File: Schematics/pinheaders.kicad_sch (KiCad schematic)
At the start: 20 parts, among them J1001 Conn_01x08_Pin, J1002 Conn_01x08_Pin, J1003 Conn_01x08_Pin, J1004 Conn_01x08_Pin, J1005 Conn_01x08_Pin, J1006 Conn_01x16_Pin, J1007 Conn_01x16_Pin, J1008 Conn_01x08_Pin, J1009 Conn_01x08_Pin, J1010 Conn_01x08_Pin, J1011 Conn_01x08_Pin, J1012 Conn_01x08_Pin, J1013 Conn_01x08_Pin, J1014 Conn_01x08_Pin, J1015 Conn_01x08_Pin, J1016 Conn_01x08_Pin, J1017 Conn_01x08_Pin, J1018 Conn_01x08_Pin, J1019 Conn_01x08_Pin, J1020 Conn_01x08_Pin

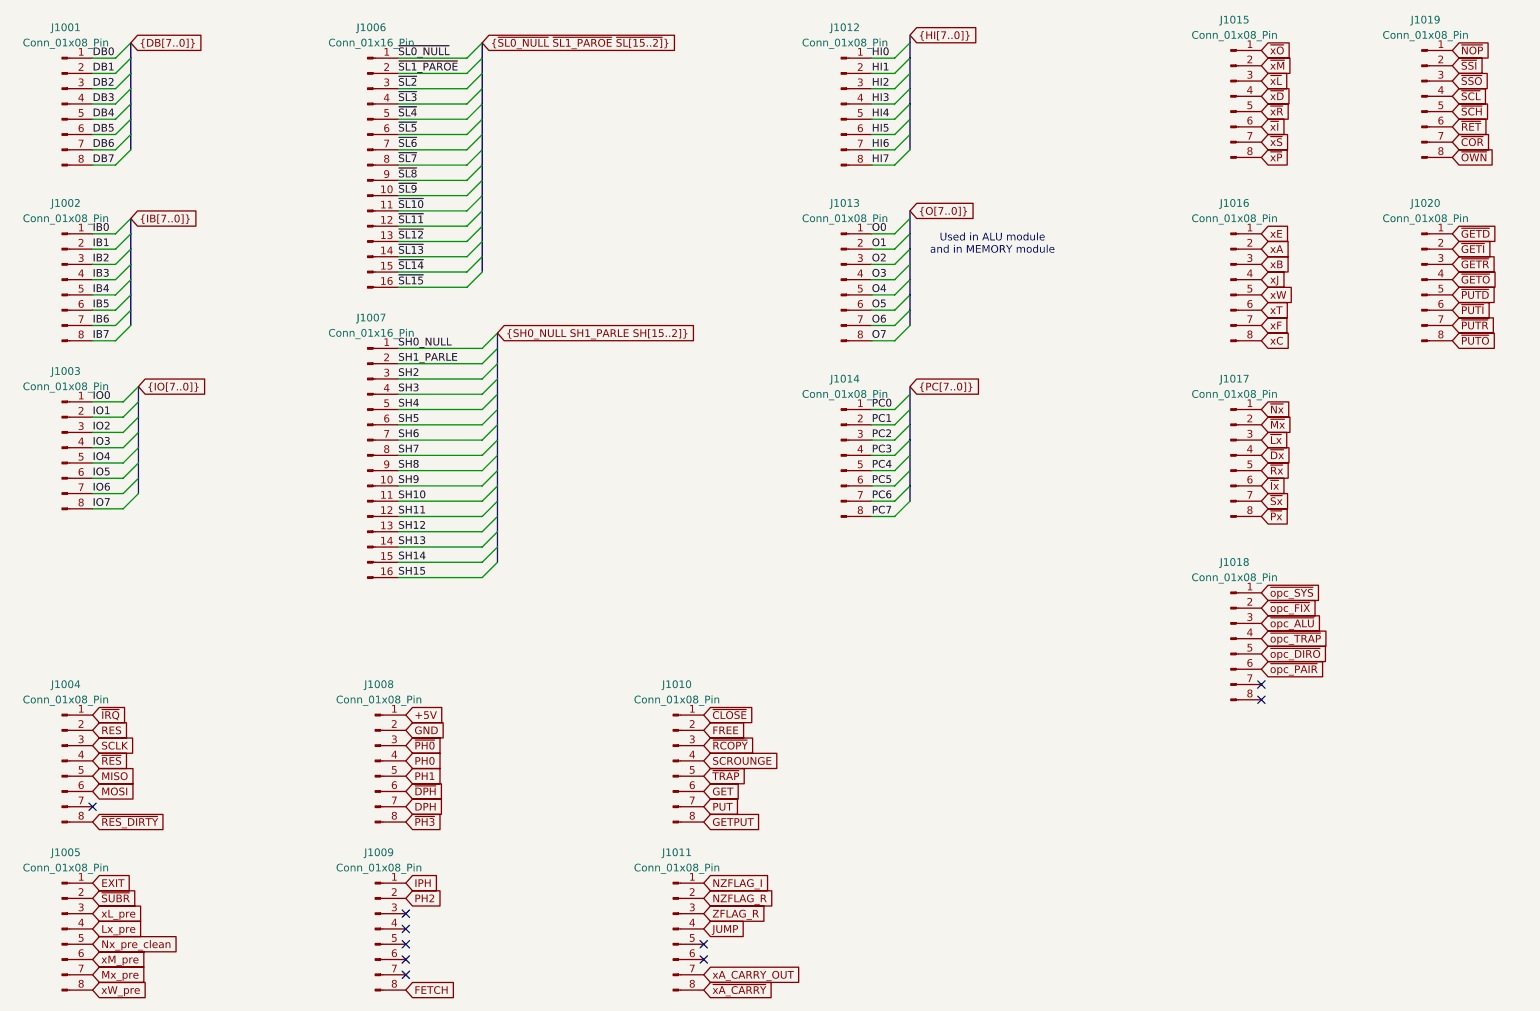
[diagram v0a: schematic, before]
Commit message: Reduce number of shared headers
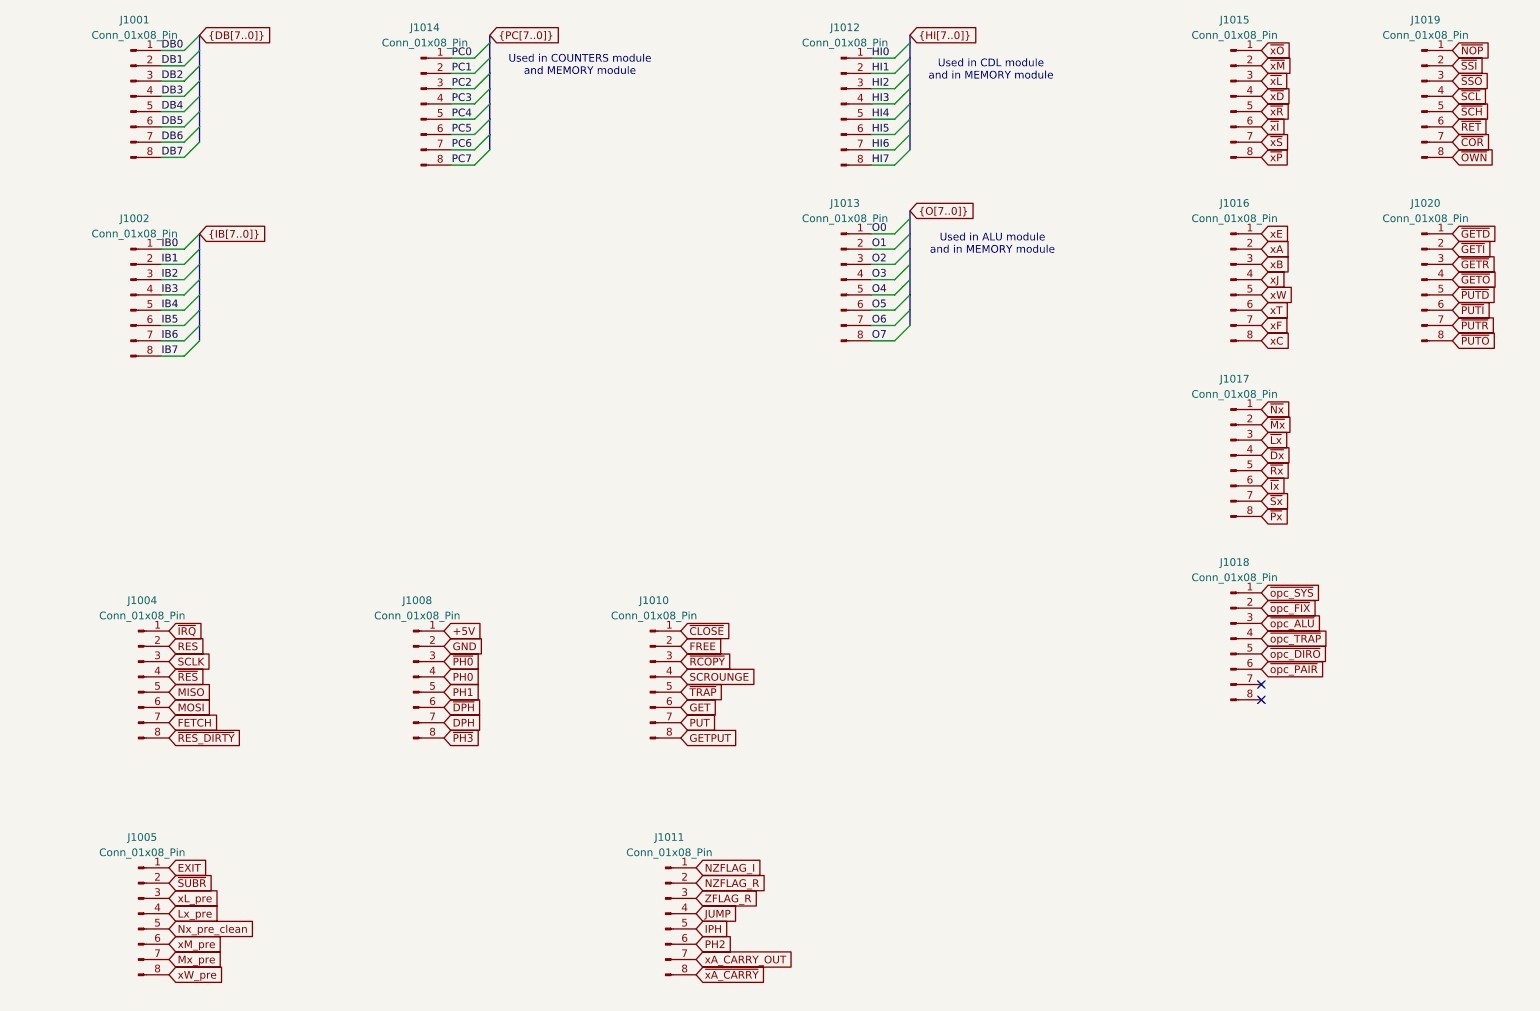
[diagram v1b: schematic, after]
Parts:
- removed J1003: Conn_01x08_Pin, symbol Connector:Conn_01x08_Pin
- removed J1006, J1007: Conn_01x16_Pin, Connector_PinHeader_2.54mm:PinHeader_1x16_P2.54mm_Vertical, symbol Connector:Conn_01x16_Pin
- removed J1009: Conn_01x08_Pin, Connector_PinHeader_2.54mm:PinHeader_1x08_P2.54mm_Vertical, symbol Connector:Conn_01x08_Pin
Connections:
- net FETCH: now also J1004.7 (Pin_7)
- net IPH: now also J1011.5 (Pin_5)
- net PH2: now also J1011.6 (Pin_6)
- no-connect marks 10 -> 2
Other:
- note added: "Used in CDL module and in MEMORY module"
- note added: "Used in COUNTERS module and MEMORY module"
- moved on the sheet: J1001, J1002, J1004, J1005, J1008, J1010, J1011, J1014

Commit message: Change d to g
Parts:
- J1001, J1002, J1004, J1008, J1010, J1011, J1012, J1014, J1015, J1016, J1017, J1018, J1019, J1020: footprint (none) -> Connector_PinHeader_2.54mm:PinHeader_1x08_P2.54mm_Vertical
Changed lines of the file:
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@@
 			)
 		)
-		(property "Footprint" ""
+		(property "Footprint" "Connector_PinHeader_2.54mm:PinHeader_1x08_P2.54mm_Vertical"
 			(at 220.98 31.75 0)
 			(effects
@@
 			(project "myth_decoder"
 				(path "/cc431572-b987-4113-b719-2952a6ee3168/4a47d886-11a5-4437-bd08-9d99b37632a9"
-					(reference "J1015")
+					(reference "J1011")
 					(unit 1)
 				)
@@
 			)
 		)
-		(property "Footprint" ""
+		(property "Footprint" "Connector_PinHeader_2.54mm:PinHeader_1x08_P2.54mm_Vertical"
 			(at 127 167.64 0)
 			(effects
@@
 			(project "myth_decoder"
 				(path "/cc431572-b987-4113-b719-2952a6ee3168/4a47d886-11a5-4437-bd08-9d99b37632a9"
-					(reference "J1011")
+					(reference "J1008")
 					(unit 1)
 				)
@@
 			)
 		)
-		(property "Footprint" ""
+		(property "Footprint" "Connector_PinHeader_2.54mm:PinHeader_1x08_P2.54mm_Vertical"
 			(at 220.98 62.23 0)
 			(effects
@@
 			(project "myth_decoder"
 				(path "/cc431572-b987-4113-b719-2952a6ee3168/4a47d886-11a5-4437-bd08-9d99b37632a9"
-					(reference "J1016")
+					(reference "J1012")
 					(unit 1)
 				)
@@
 			)
 		)
-		(property "Footprint" ""
+		(property "Footprint" "Connector_PinHeader_2.54mm:PinHeader_1x08_P2.54mm_Vertical"
 			(at 85.09 128.27 0)
 			(effects
@@
 			(project "myth_decoder"
 				(path "/cc431572-b987-4113-b719-2952a6ee3168/4a47d886-11a5-4437-bd08-9d99b37632a9"
-					(reference "J1008")
+					(reference "J1005")
 					(unit 1)
 				)
@@
 			)
 		)
-		(property "Footprint" ""
+		(property "Footprint" "Connector_PinHeader_2.54mm:PinHeader_1x08_P2.54mm_Vertical"
 			(at 38.1 31.75 0)
 			(effects
@@
 			)
 		)
-		(property "Footprint" ""
+		(property "Footprint" "Connector_PinHeader_2.54mm:PinHeader_1x08_P2.54mm_Vertical"
 			(at 38.1 64.77 0)
 			(effects
@@
 			)
 		)
-		(property "Footprint" ""
+		(property "Footprint" "Connector_PinHeader_2.54mm:PinHeader_1x08_P2.54mm_Vertical"
 			(at 252.73 31.75 0)
 			(effects
@@
 			(project "myth_decoder"
 				(path "/cc431572-b987-4113-b719-2952a6ee3168/4a47d886-11a5-4437-bd08-9d99b37632a9"
-					(reference "J1019")
+					(reference "J1015")
 					(unit 1)
 				)
@@
 			)
 		)
-		(property "Footprint" ""
+		(property "Footprint" "Connector_PinHeader_2.54mm:PinHeader_1x08_P2.54mm_Vertical"
 			(at 124.46 128.27 0)
 			(effects
@@
 			(project "myth_decoder"
 				(path "/cc431572-b987-4113-b719-2952a6ee3168/4a47d886-11a5-4437-bd08-9d99b37632a9"
-					(reference "J1010")
+					(reference "J1007")
 					(unit 1)
 				)
@@
 			)
 		)
-		(property "Footprint" ""
+		(property "Footprint" "Connector_PinHeader_2.54mm:PinHeader_1x08_P2.54mm_Vertical"
 			(at 220.98 91.44 0)
 			(effects
@@
 			(project "myth_decoder"
 				(path "/cc431572-b987-4113-b719-2952a6ee3168/4a47d886-11a5-4437-bd08-9d99b37632a9"
-					(reference "J1017")
+					(reference "J1013")
 					(unit 1)
 				)
@@
 			)
 		)
-		(property "Footprint" ""
+		(property "Footprint" "Connector_PinHeader_2.54mm:PinHeader_1x08_P2.54mm_Vertical"
 			(at 156.21 33.02 0)
 			(effects
@@
 			(project "myth_decoder"
 				(path "/cc431572-b987-4113-b719-2952a6ee3168/4a47d886-11a5-4437-bd08-9d99b37632a9"
-					(reference "J1012")
+					(reference "J1009")
 					(unit 1)
 				)
@@
 			)
 		)
-		(property "Footprint" ""
+		(property "Footprint" "Connector_PinHeader_2.54mm:PinHeader_1x08_P2.54mm_Vertical"
 			(at 39.37 128.27 0)
 			(effects
@@
 			(project "myth_decoder"
 				(path "/cc431572-b987-4113-b719-2952a6ee3168/4a47d886-11a5-4437-bd08-9d99b37632a9"
-					(reference "J1004")
+					(reference "J1003")
 					(unit 1)
 				)
@@
 			(project "myth_decoder"
 				(path "/cc431572-b987-4113-b719-2952a6ee3168/4a47d886-11a5-4437-bd08-9d99b37632a9"
-					(reference "J1005")
+					(reference "J1004")
 					(unit 1)
 				)
@@
 			)
 		)
-		(property "Footprint" ""
+		(property "Footprint" "Connector_PinHeader_2.54mm:PinHeader_1x08_P2.54mm_Vertical"
 			(at 220.98 121.92 0)
 			(effects
@@
 			(project "myth_decoder"
 				(path "/cc431572-b987-4113-b719-2952a6ee3168/4a47d886-11a5-4437-bd08-9d99b37632a9"
-					(reference "J1018")
+					(reference "J1014")
 					(unit 1)
 				)
@@
 			(project "myth_decoder"
 				(path "/cc431572-b987-4113-b719-2952a6ee3168/4a47d886-11a5-4437-bd08-9d99b37632a9"
-					(reference "J1013")
+					(reference "J1010")
 					(unit 1)
 				)
@@
 			)
 		)
-		(property "Footprint" ""
+		(property "Footprint" "Connector_PinHeader_2.54mm:PinHeader_1x08_P2.54mm_Vertical"
 			(at 252.73 62.23 0)
 			(effects
@@
 			(project "myth_decoder"
 				(path "/cc431572-b987-4113-b719-2952a6ee3168/4a47d886-11a5-4437-bd08-9d99b37632a9"
-					(reference "J1020")
+					(reference "J1016")
 					(unit 1)
 				)
@@
 			)
 		)
-		(property "Footprint" ""
+		(property "Footprint" "Connector_PinHeader_2.54mm:PinHeader_1x08_P2.54mm_Vertical"
 			(at 86.36 33.02 0)
 			(effects
@@
 			(project "myth_decoder"
 				(path "/cc431572-b987-4113-b719-2952a6ee3168/4a47d886-11a5-4437-bd08-9d99b37632a9"
-					(reference "J1014")
-					(unit 1)
-				)
+					(reference "J1006")
+					(unit 1)
+				)

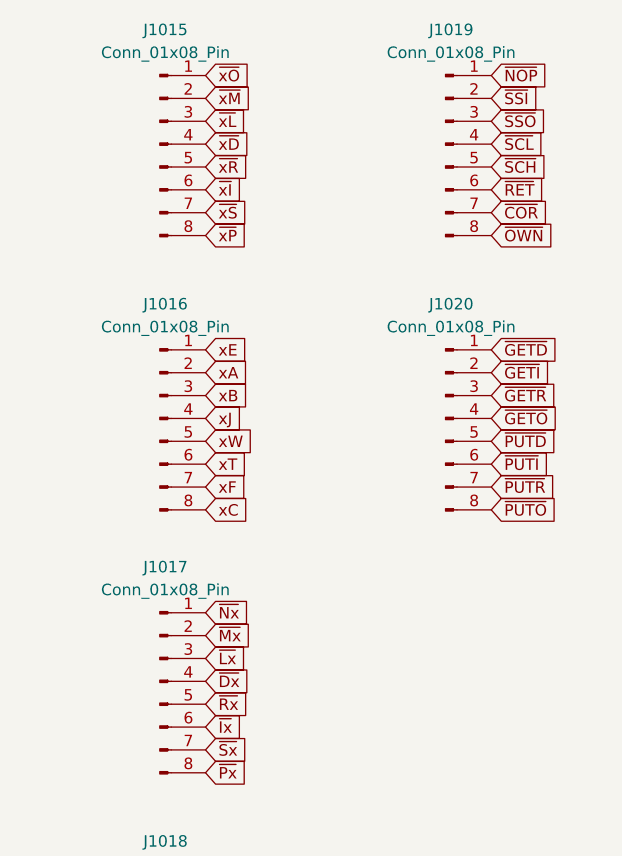
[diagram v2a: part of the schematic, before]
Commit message: Change CO do D
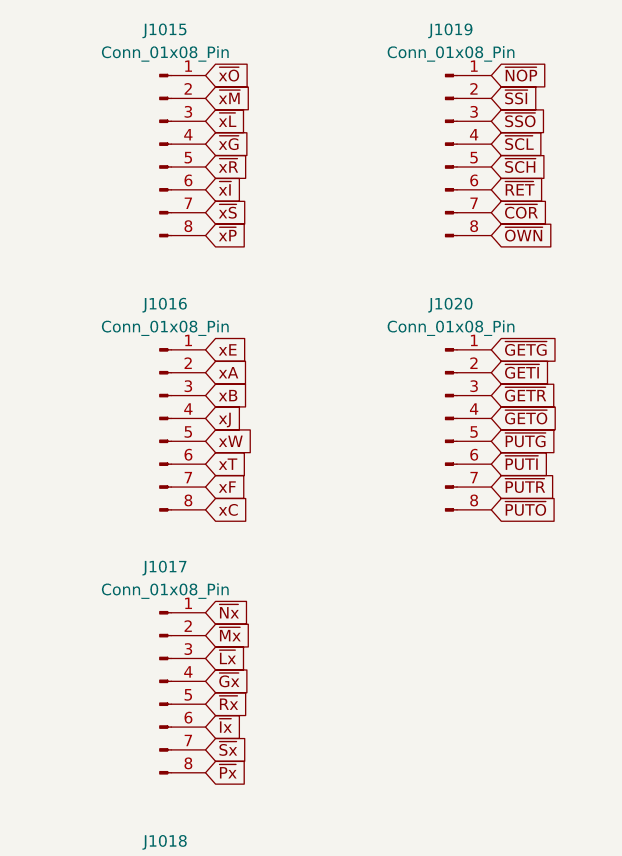
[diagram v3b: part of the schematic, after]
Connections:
- net ~{Dx} renamed ~{Gx}
- net ~{GETD} renamed ~{GETG}
- net ~{PUTD} renamed ~{PUTG}
- net ~{xD} renamed ~{xG}
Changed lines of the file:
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@@
 		)
 	)
-	(global_label "~{Dx}"
+	(global_label "~{Gx}"
 		(shape input)
 		(at 226.06 91.44 0)
@@
 		)
 	)
-	(global_label "~{PUTD}"
+	(global_label "~{PUTG}"
 		(shape input)
 		(at 257.81 64.77 0)
@@
 		)
 	)
-	(global_label "~{GETD}"
+	(global_label "~{GETG}"
 		(shape input)
 		(at 257.81 54.61 0)
@@
 		)
 	)
-	(global_label "~{xD}"
+	(global_label "~{xG}"
 		(shape input)
 		(at 226.06 31.75 0)
@@
 			(project "myth_io"
 				(path "/a907dd88-e0e4-4e6e-a291-053f6213a316/95b8575f-ea13-4da8-aaa7-78fdcde116f0"
-					(reference "J1011")
+					(reference "J1012")
 					(unit 1)
 				)
@@
 			(project "myth_io"
 				(path "/a907dd88-e0e4-4e6e-a291-053f6213a316/95b8575f-ea13-4da8-aaa7-78fdcde116f0"
-					(reference "J1008")
+					(reference "J1009")
 					(unit 1)
 				)
@@
 			(project "myth_io"
 				(path "/a907dd88-e0e4-4e6e-a291-053f6213a316/95b8575f-ea13-4da8-aaa7-78fdcde116f0"
-					(reference "J1001")
+					(reference "J1005")
 					(unit 1)
 				)
@@
 			(project "myth_io"
 				(path "/a907dd88-e0e4-4e6e-a291-053f6213a316/95b8575f-ea13-4da8-aaa7-78fdcde116f0"
-					(reference "J1002")
+					(reference "J1006")
 					(unit 1)
 				)
@@
 			(project "myth_io"
 				(path "/a907dd88-e0e4-4e6e-a291-053f6213a316/95b8575f-ea13-4da8-aaa7-78fdcde116f0"
-					(reference "J1010")
+					(reference "J1011")
 					(unit 1)
 				)
@@
 			(project "myth_io"
 				(path "/a907dd88-e0e4-4e6e-a291-053f6213a316/95b8575f-ea13-4da8-aaa7-78fdcde116f0"
-					(reference "J1012")
+					(reference "J1013")
 					(unit 1)
 				)
@@
 			(project "myth_io"
 				(path "/a907dd88-e0e4-4e6e-a291-053f6213a316/95b8575f-ea13-4da8-aaa7-78fdcde116f0"
-					(reference "J1004")
+					(reference "J1007")
 					(unit 1)
 				)
@@
 			(project "myth_io"
 				(path "/a907dd88-e0e4-4e6e-a291-053f6213a316/95b8575f-ea13-4da8-aaa7-78fdcde116f0"
-					(reference "J1005")
+					(reference "J1008")
 					(unit 1)
 				)
@@
 			(project "myth_io"
 				(path "/a907dd88-e0e4-4e6e-a291-053f6213a316/95b8575f-ea13-4da8-aaa7-78fdcde116f0"
-					(reference "J1013")
+					(reference "J1014")
 					(unit 1)
 				)
@@
 			(project "myth_io"
 				(path "/a907dd88-e0e4-4e6e-a291-053f6213a316/95b8575f-ea13-4da8-aaa7-78fdcde116f0"
-					(reference "J1014")
+					(reference "J1010")
 					(unit 1)
 				)
